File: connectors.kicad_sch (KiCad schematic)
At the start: 4 parts, among them J1 Conn_01x04_Pin, J2 Conn_01x04_Pin, J3 Conn_01x09_Pin, J4 Conn_02x03_Odd_Even

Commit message: Footprints associated
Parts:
- J1, J2: footprint (none) -> Connector_PinHeader_2.54mm:PinHeader_1x04_P2.54mm_Vertical
- J3: footprint (none) -> Connector_PinHeader_2.54mm:PinHeader_1x09_P2.54mm_Vertical
- J4: footprint (none) -> Connector_PinHeader_2.54mm:PinHeader_2x03_P2.54mm_Vertical
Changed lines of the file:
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@@
 			)
 		)
-		(property "Footprint" ""
+		(property "Footprint" "Connector_PinHeader_2.54mm:PinHeader_2x03_P2.54mm_Vertical"
 			(at 90.17 76.2 0)
 			(effects
@@
 			)
 		)
-		(property "Footprint" ""
+		(property "Footprint" "Connector_PinHeader_2.54mm:PinHeader_1x04_P2.54mm_Vertical"
 			(at 58.42 48.26 0)
 			(effects
@@
 			)
 		)
-		(property "Footprint" ""
+		(property "Footprint" "Connector_PinHeader_2.54mm:PinHeader_1x09_P2.54mm_Vertical"
 			(at 58.42 80.01 0)
 			(effects
@@
 			)
 		)
-		(property "Footprint" ""
+		(property "Footprint" "Connector_PinHeader_2.54mm:PinHeader_1x04_P2.54mm_Vertical"
 			(at 87.63 48.26 0)
 			(effects

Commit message: wiring has been done
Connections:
- net MISO: now reaches J4.1 (Pin_1)
- net VCC: now reaches J4.2 (Pin_2)
- net VCC: now also J1.2 (Pin_2), J2.2 (Pin_2), J3.9 (Pin_9)
- net SCK: now reaches J4.3 (Pin_3)
- net SCK: now also J1.4 (Pin_4)
- net MOSI: now reaches J4.4 (Pin_4)
- net RESET: now reaches J4.5 (Pin_5)
- net GND: now reaches J4.6 (Pin_6)
- net GND: now also J1.1 (Pin_1), J2.1 (Pin_1), J3.8 (Pin_8)
- net SDA: now reaches J1.3 (Pin_3)
- net D2: now reaches J3.1 (Pin_1)
- net D3: now reaches J3.2 (Pin_2)
- net D4: now reaches J3.3 (Pin_3)
- net D5: now reaches J3.4 (Pin_4)
- net D6: now reaches J3.5 (Pin_5)
- net D7: now reaches J3.6 (Pin_6)
- net D8: now reaches J3.7 (Pin_7)
- net RX: now reaches J2.3 (Pin_3)
- net TX: now reaches J2.4 (Pin_4)
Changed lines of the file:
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@@
 	(generator_version "9.0")
 	(paper "A4")
+	(hierarchical_label "VCC"
+		(shape passive)
+		(at 92.71 48.26 0)
+		(effects
+			(font
+				(size 1.27 1.27)
+			)
+			(justify left)
+		)
+	)
+	(hierarchical_label "SCK"
+		(shape bidirectional)
+		(at 85.09 76.2 180)
+		(effects
+			(font
+				(size 1.27 1.27)
+			)
+			(justify right)
+		)
+	)
+	(hierarchical_label "D5"
+		(shape bidirectional)
+		(at 63.5 77.47 0)
+		(effects
+			(font
+				(size 1.27 1.27)
+			)
+			(justify left)
+		)
+	)
+	(hierarchical_label "SCK"
+		(shape bidirectional)
+		(at 63.5 53.34 0)
+		(effects
+			(font
+				(size 1.27 1.27)
+			)
+			(justify left)
+		)
+	)
+	(hierarchical_label "MOSI"
+		(shape input)
+		(at 97.79 76.2 0)
+		(effects
+			(font
+				(size 1.27 1.27)
+			)
+			(justify left)
+		)
+	)
+	(hierarchical_label "D3"
+		(shape bidirectional)
+		(at 63.5 72.39 0)
+		(effects
+			(font
+				(size 1.27 1.27)
+			)
+			(justify left)
+		)
+	)
+	(hierarchical_label "VCC"
+		(shape passive)
+		(at 63.5 48.26 0)
+		(effects
+			(font
+				(size 1.27 1.27)
+			)
+			(justify left)
+		)
+	)
+	(hierarchical_label "D6"
+		(shape bidirectional)
+		(at 63.5 80.01 0)
+		(effects
+			(font
+				(size 1.27 1.27)
+			)
+			(justify left)
+		)
+	)
+	(hierarchical_label "D8"
+		(shape bidirectional)
+		(at 63.5 85.09 0)
+		(effects
+			(font
+				(size 1.27 1.27)
+			)
+			(justify left)
+		)
+	)
+	(hierarchical_label "VCC"
+		(shape passive)
+		(at 63.5 90.17 0)
+		(effects
+			(font
+				(size 1.27 1.27)
+			)
+			(justify left)
+		)
+	)
+	(hierarchical_label "VCC"
+		(shape passive)
+		(at 97.79 73.66 0)
+		(effects
+			(font
+				(size 1.27 1.27)
+			)
+			(justify left)
+		)
+	)
+	(hierarchical_label "SDA"
+		(shape bidirectional)
+		(at 63.5 50.8 0)
+		(effects
+			(font
+				(size 1.27 1.27)
+			)
+			(justify left)
+		)
+	)
+	(hierarchical_label "GND"
+		(shape passive)
+		(at 63.5 87.63 0)
+		(effects
+			(font
+				(size 1.27 1.27)
+			)
+			(justify left)
+		)
+	)
+	(hierarchical_label "GND"
+		(shape passive)
+		(at 92.71 45.72 0)
+		(effects
+			(font
+				(size 1.27 1.27)
+			)
+			(justify left)
+		)
+	)
+	(hierarchical_label "RESET"
+		(shape passive)
+		(at 85.09 78.74 180)
+		(effects
+			(font
+				(size 1.27 1.27)
+			)
+			(justify right)
+		)
+	)
+	(hierarchical_label "D4"
+		(shape bidirectional)
+		(at 63.5 74.93 0)
+		(effects
+			(font
+				(size 1.27 1.27)
+			)
+			(justify left)
+		)
+	)
+	(hierarchical_label "RX"
+		(shape input)
+		(at 92.71 50.8 0)
+		(effects
+			(font
+				(size 1.27 1.27)
+			)
+			(justify left)
+		)
+	)
+	(hierarchical_label "D2"
+		(shape bidirectional)
+		(at 63.5 69.85 0)
+		(effects
+			(font
+				(size 1.27 1.27)
+			)
+			(justify left)
+		)
+	)
+	(hierarchical_label "MISO"
+		(shape output)
+		(at 85.09 73.66 180)
+		(effects
+			(font
+				(size 1.27 1.27)
+			)
+			(justify right)
+		)
+	)
+	(hierarchical_label "GND"
+		(shape passive)
+		(at 63.5 45.72 0)
+		(effects
+			(font
+				(size 1.27 1.27)
+			)
+			(justify left)
+		)
+	)
+	(hierarchical_label "TX"
+		(shape output)
+		(at 92.71 53.34 0)
+		(effects
+			(font
+				(size 1.27 1.27)
+			)
+			(justify left)
+		)
+	)
+	(hierarchical_label "GND"
+		(shape passive)
+		(at 97.79 78.74 0)
+		(effects
+			(font
+				(size 1.27 1.27)
+			)
+			(justify left)
+		)
+	)
+	(hierarchical_label "D7"
+		(shape bidirectional)
+		(at 63.5 82.55 0)
+		(effects
+			(font
+				(size 1.27 1.27)
+			)
+			(justify left)
+		)
+	)
 	(symbol
 		(lib_id "Connector_Generic:Conn_02x03_Odd_Even")

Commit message: Fixed a defect
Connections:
- net SCK: no longer J1.4 (Pin_4)
- new net SCL: J1.4 (Pin_4)
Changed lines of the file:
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@@
 		)
 	)
-	(hierarchical_label "SCK"
+	(hierarchical_label "SCL"
 		(shape bidirectional)
 		(at 63.5 53.34 0)

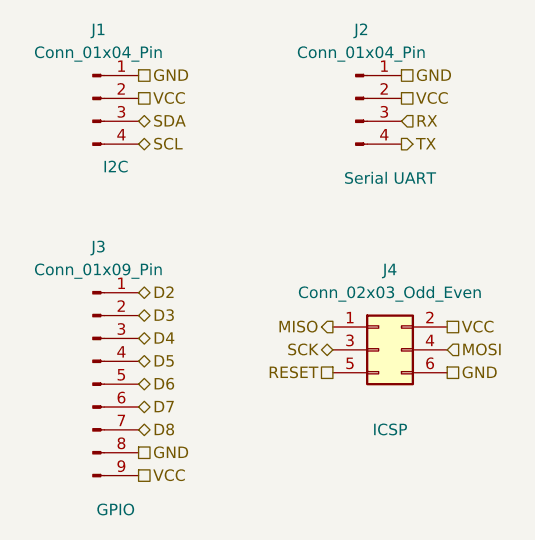
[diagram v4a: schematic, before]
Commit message: Fixed defects in schematic
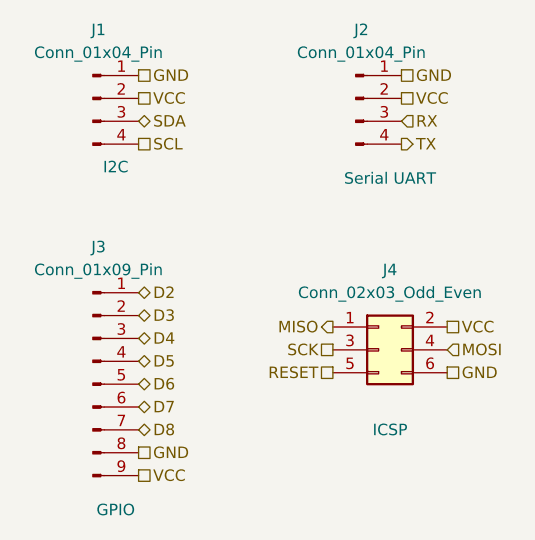
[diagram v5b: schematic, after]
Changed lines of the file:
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@@
 	)
 	(hierarchical_label "SCK"
-		(shape bidirectional)
+		(shape passive)
 		(at 85.09 76.2 180)
 		(effects
@@
 		(shape bidirectional)
 		(at 63.5 77.47 0)
-		(effects
-			(font
-				(size 1.27 1.27)
-			)
-			(justify left)
-		)
-	)
-	(hierarchical_label "SCL"
-		(shape bidirectional)
-		(at 63.5 53.34 0)
 		(effects
 			(font
@@
 		(effects
 			(font
+				(size 1.27 1.27)
+			)
+			(justify left)
+		)
+	)
+	(hierarchical_label "SCL"
+		(shape passive)
+		(at 63.5 53.34 0)
+		(effects
+			(font
